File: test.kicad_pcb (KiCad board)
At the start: 4 copper layers, 100 x 50 mm, 116 parts, among them IC1 USBLC6-2SC6, IC2 AD9288BSTZ-40, IC3 MAX17048G+T10, IC4 BQ24074RGTR, IC5 TCA9534APWR, IC6 MCP6S91-E_MS, IC7 MCP6S91-E_MS, IC8 MCP4726A0T-E_CH, J1 PWM, K1 AQY210EHAX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

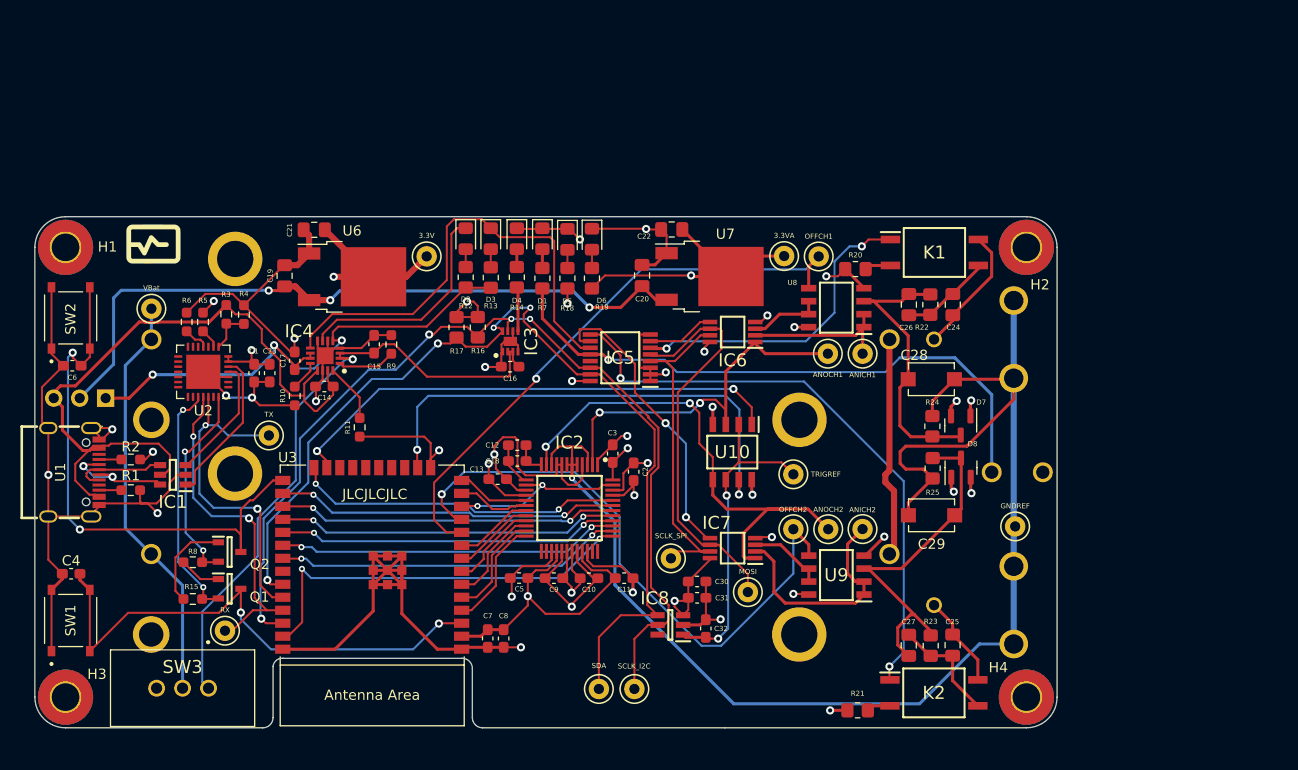
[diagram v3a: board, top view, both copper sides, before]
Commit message: changed linear regulators
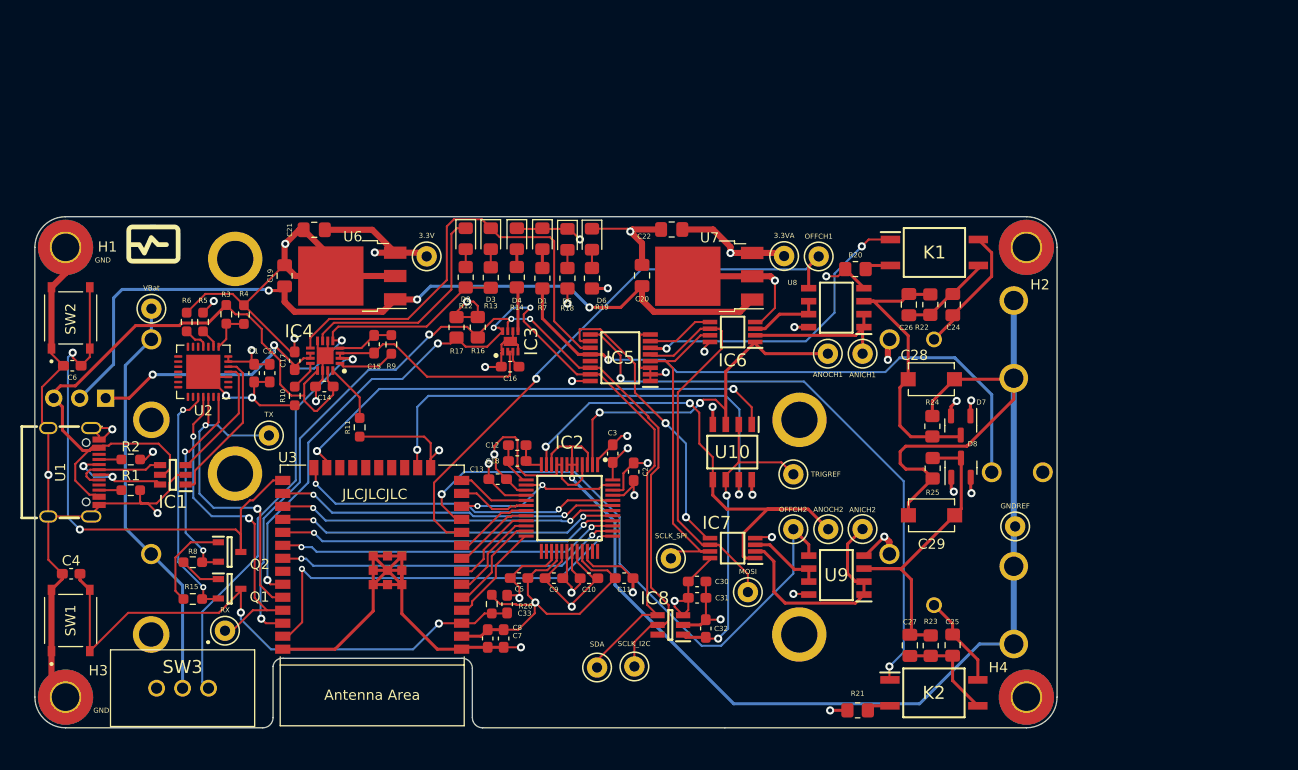
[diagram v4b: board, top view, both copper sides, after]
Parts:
- added C33: 0.1u, Capacitor_SMD:C_0603_1608Metric_Pad1.08x0.95mm_HandSolder, F.Cu at (146.2, 86.9)
- added R26: 10k, Resistor_SMD:R_0603_1608Metric_Pad0.98x0.95mm_HandSolder, F.Cu at (144.7, 86.9)
- C21, C22: value 10u -> 2.2u
- H1, H3: value MountingHole -> GND
- U6, U7: value LD1086DT33TR -> LD39150DT33; footprint Package_TO_SOT_SMD:TO-252-2 -> Package_TO_SOT_SMD:TO-252-3_TabPin2
- moved TP12 2.20 mm to (158.7, 93.0)
- moved TP13 2.11 mm to (155.0, 93.1)
- moved C27 0.11 mm to (185.6, 90.9), turned to -90 degrees
- moved U6 0.08 mm to (131.1, 54.8), turned to 180 degrees
- turned U7 to 180 degrees
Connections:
- H1 pad 1: (no net) -> GND
- H3 pad 1: (no net) -> GND
- U6 pad 1: GND -> Net-(C19-Pad1)
- U6 pad 2: +3V3 -> GND
- U6 pad 3: Net-(C19-Pad1) -> +3V3
- U7 pad 1: GND -> Net-(C19-Pad1)
- U7 pad 2: +3.3VA -> GND
- U7 pad 3: Net-(C19-Pad1) -> +3.3VA
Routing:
- net +3.3VA: track 69.4 -> 54.5 mm, vias 10 -> 11
- net Net-(C19-Pad1): track 68.8 -> 80.6 mm
- net GND: track 324.5 -> 330.9 mm, vias 29 -> 31
- net ENABLE: track 52.2 -> 56.8 mm
- net SDA: track 96.1 -> 92.1 mm
- net SCL_I2C: track 97.2 -> 94.0 mm
- net /CH2_D0: track 11.0 -> 9.62 mm
- net Net-(C25-Pad1): track 11.1 -> 12.2 mm
- net /CH2_D1: track 10.5 -> 9.41 mm
- net +5V: track 70.3 -> 69.3 mm
- net CH1_AC_Sel: track 30.9 -> 30.1 mm
- net Net-(C17-Pad1): track 52.7 -> 51.9 mm
- net RX: track 32.8 -> 32.0 mm
- net Net-(K2-Pad2): track 2.34 -> 1.72 mm
- net Net-(C32-Pad1): track 31.4 -> 30.8 mm
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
